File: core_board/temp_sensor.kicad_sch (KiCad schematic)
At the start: 0 parts

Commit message: Add temp sensor
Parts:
- added C11: 100nF, MRDT_Shields:RoveNode_H5, symbol Device:C
- added R7: 10kohm, Package_SO:TSSOP-20_4.4x6.5mm_P0.65mm, symbol Device:R_US
- added TH1: Thermistor_NTC, Package_DFN_QFN:Nordic_AQFN-94-1EP_7x7mm_P0.4mm, symbol Device:Thermistor_NTC
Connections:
- new net +3V3: R7.1
- new net GND: C11.2, TH1.2
- new net TEMP_OUT: C11.1, R7.2, TH1.1

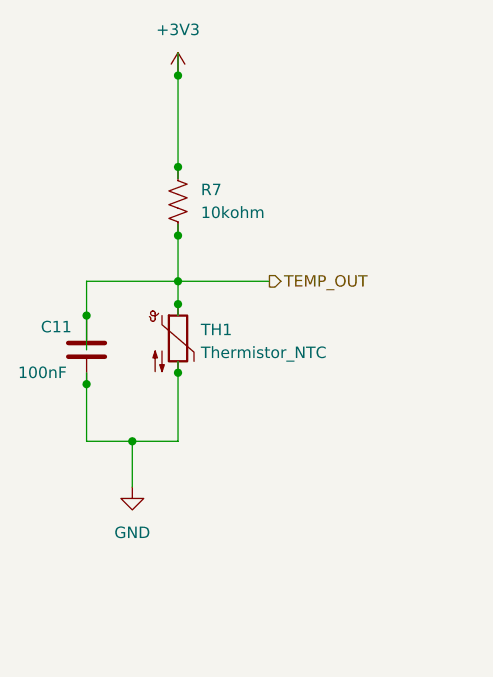
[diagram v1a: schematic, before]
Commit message: add temp sensor datasheet
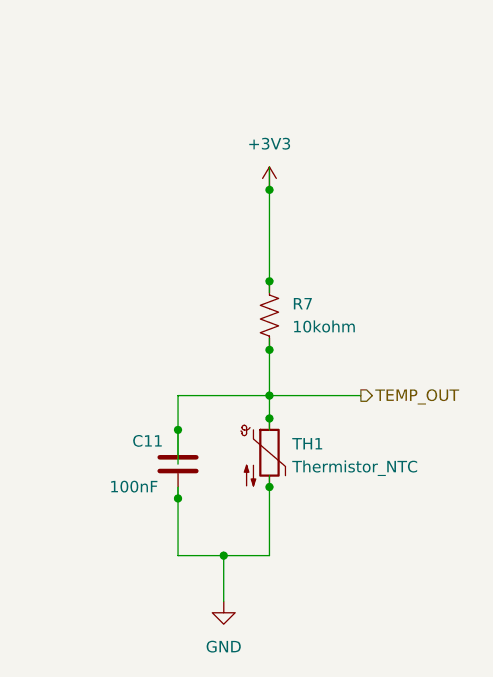
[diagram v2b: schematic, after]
